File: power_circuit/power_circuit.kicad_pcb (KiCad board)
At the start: 2 copper layers, 16 parts, among them J1 +, J10 Conn_01x02_Pin, J2 -, J7 Conn_01x02_Pin, J8 Conn_01x02_Pin, J9 Conn_01x02_Pin, U1 LM76002RNPR, U2 STM32F042C6Tx, U3 TJA1051TK-3

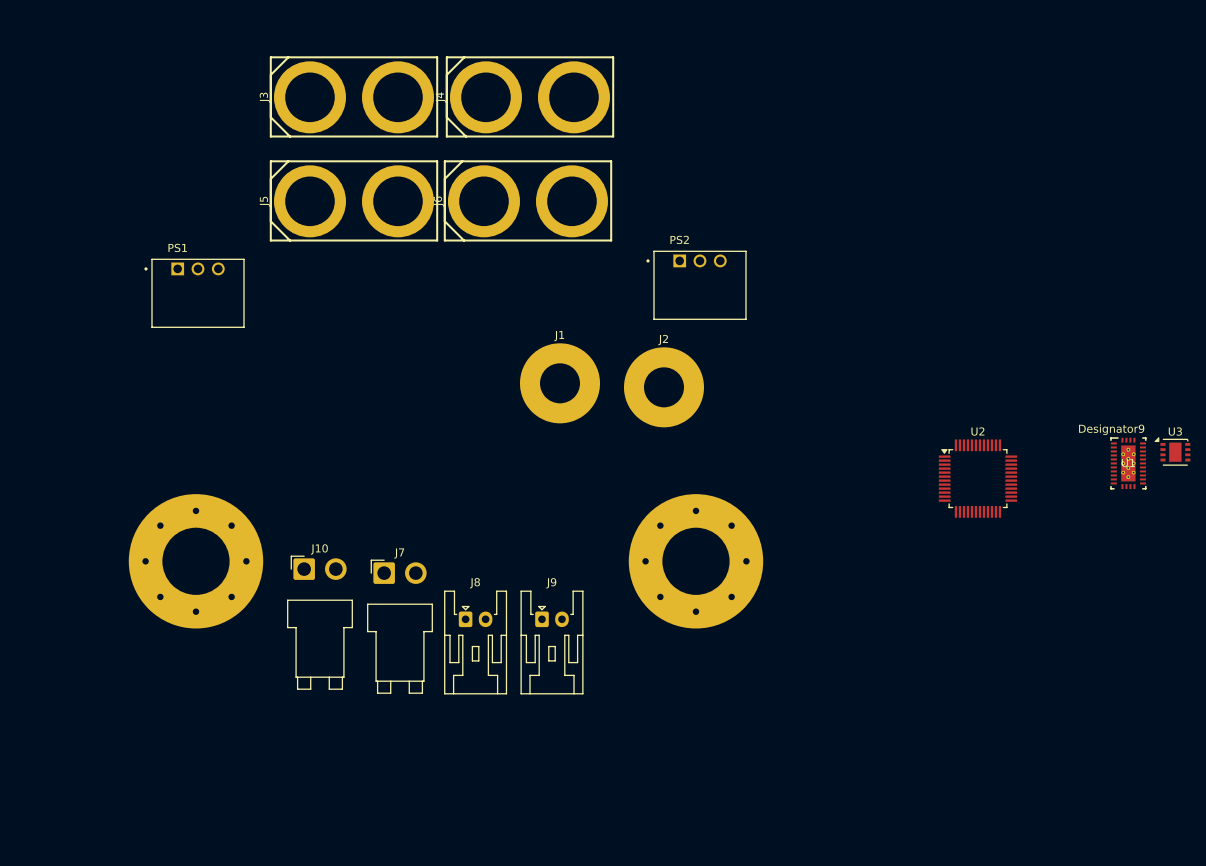
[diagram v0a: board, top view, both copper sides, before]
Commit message: AQUA_VESC REV01作成
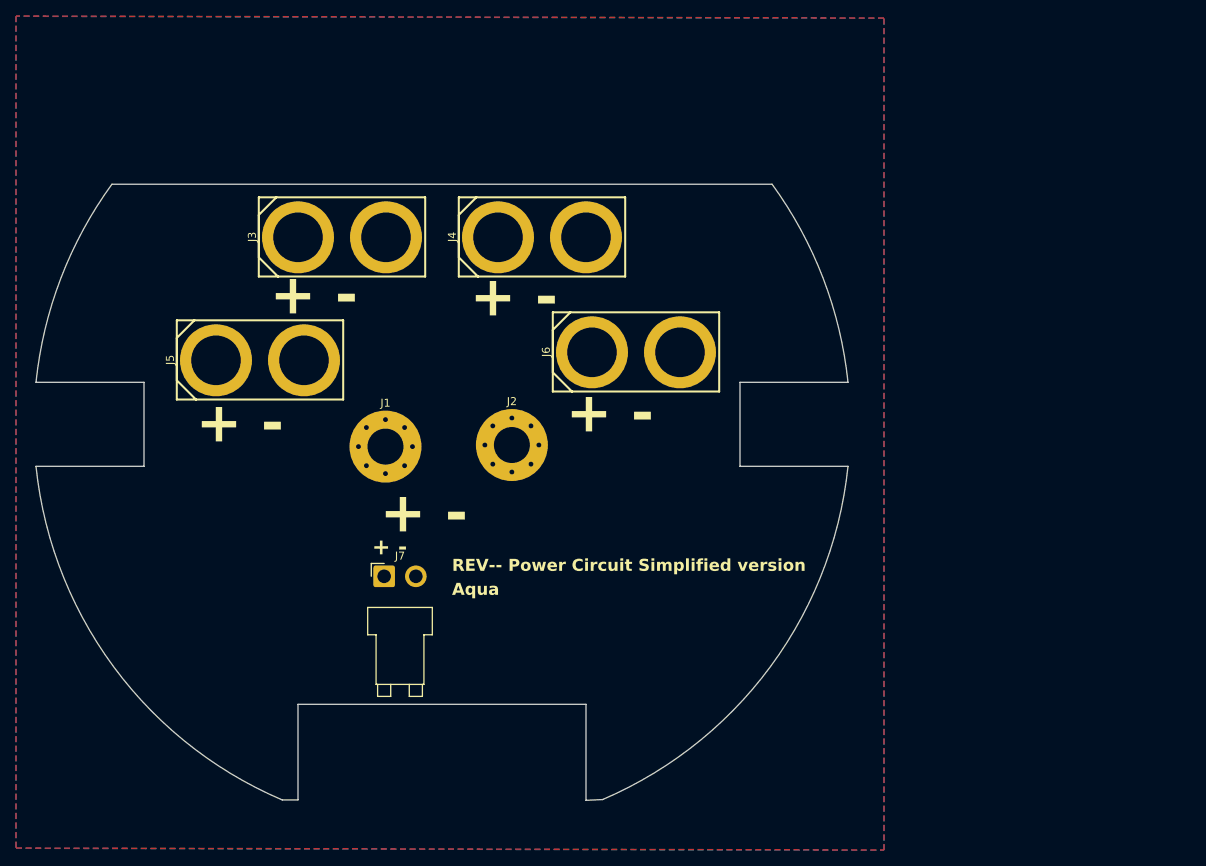
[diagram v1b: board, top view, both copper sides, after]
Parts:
- removed F1: Fuse, specific_footprint_library:anl_fuse
- removed J10: Conn_01x02_Pin, Connector_JST:JST_VH_B2PS-VH_1x02_P3.96mm_Horizontal
- removed J8, J9: Conn_01x02_Pin, Connector_JST:JST_XA_S02B-XASK-1_1x02_P2.50mm_Horizontal
- removed PS1, PS2: R-78K12-2.0, specific_footprint_library:CONV_R-78K12-2.0
- removed U1: LM76002RNPR, specific_footprint_library:RNP0030B
- removed U2: STM32F042C6Tx, Package_QFP:LQFP-48_7x7mm_P0.5mm
- removed U3: TJA1051TK-3, Package_DFN_QFN:DFN-8-1EP_3x3mm_P0.65mm_EP1.55x2.4mm
- J1: value + -> Conn_01x01_Pin; footprint MountingHole:MountingHole_5mm_Pad -> MountingHole:MountingHole_4.5mm_Pad_Via
- J2: footprint MountingHole:MountingHole_5mm_Pad -> MountingHole:MountingHole_4.5mm_Pad_Via
- moved J6 23.2 mm to (94.5, 55.6)
- moved J1 23.2 mm to (63.2, 67.4)
- moved J5 23.1 mm to (47.5, 56.6)
- moved J2 20.3 mm to (79.0, 67.2)
- moved J3 17.6 mm to (57.8, 41.2)
- moved J4 17.6 mm to (82.8, 41.2)
- moved J7 0.40 mm to (63.0, 83.6)
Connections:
- J1 pad 1: Net-(J1-Pin_1) -> +24V
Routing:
- added copper zone on F.Cu, net +24V
- added copper zone on B.Cu, net GND
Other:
- board outline added: 101.5 x 77 mm
- board text added: "+ -"
- board text added: "Aqua"
- board text added: "REV-- Power Circuit Simplified version"
